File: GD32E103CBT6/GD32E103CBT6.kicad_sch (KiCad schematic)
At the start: 15 parts, among them J1 DBG, U1 GD32E103CBTx, Y1 16MHz

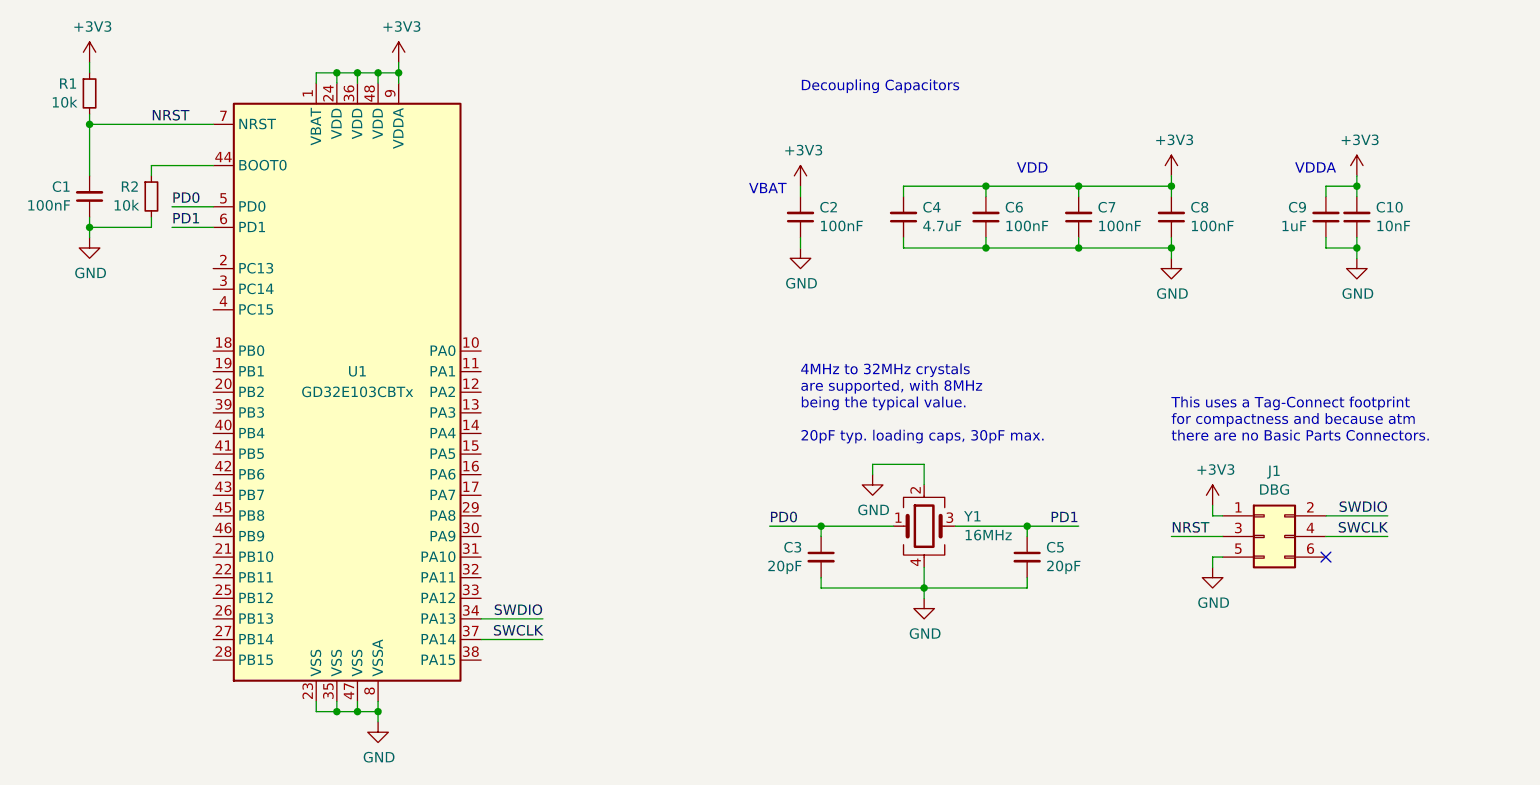
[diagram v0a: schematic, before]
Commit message: Revert "Update modules to kicad v7 format"
This reverts commit 3325eb02d48d3d222bc7f8945228a1814ae85736.
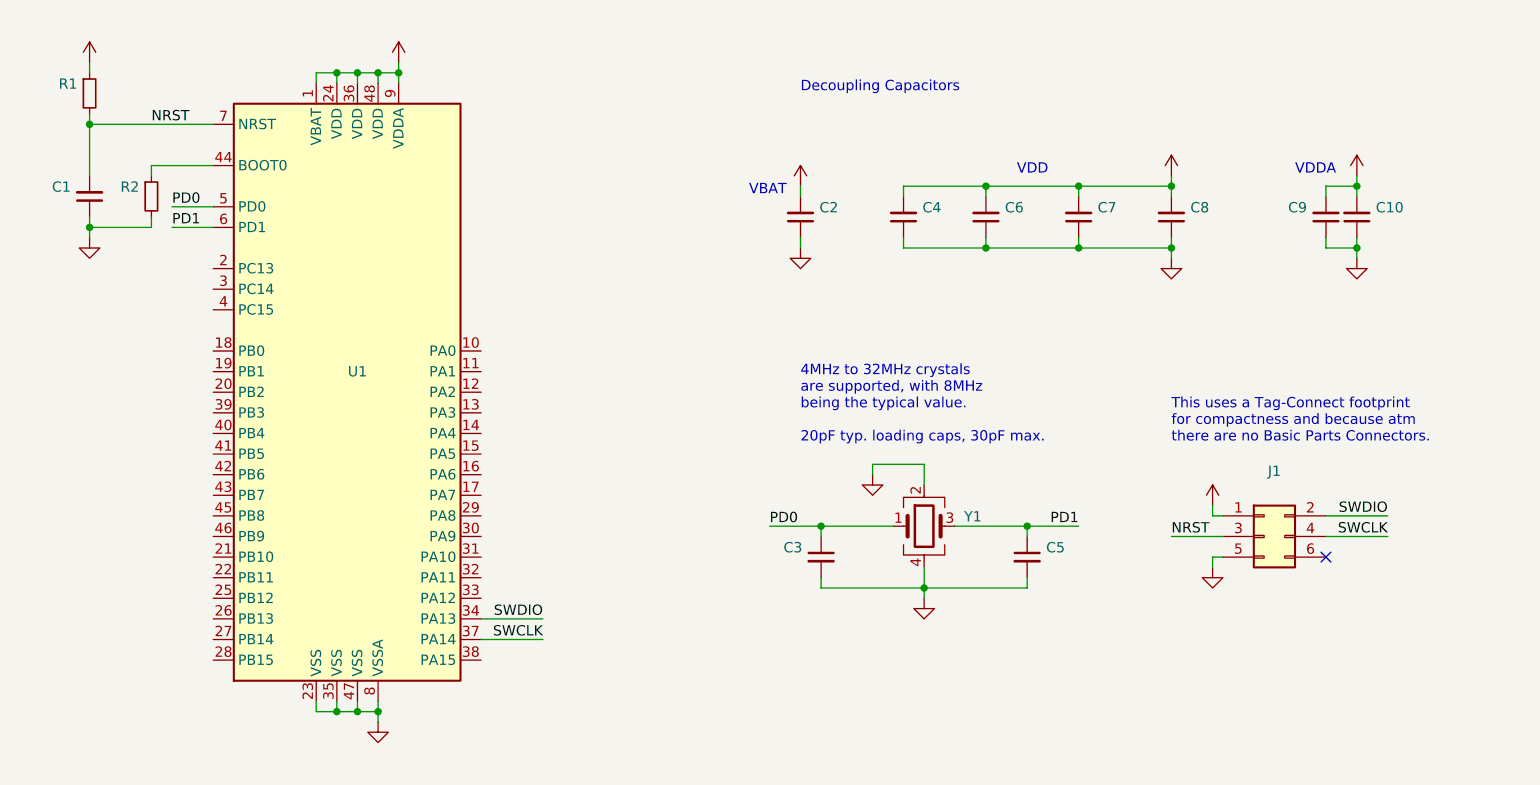
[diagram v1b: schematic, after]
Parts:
- C1, C2, C6, C7, C8: value 100nF -> (none); footprint Capacitor_SMD:C_0402_1005Metric -> (none)
- C10: value 10nF -> (none); footprint Capacitor_SMD:C_0402_1005Metric -> (none)
- C3, C5: value 20pF -> (none); footprint Capacitor_SMD:C_0402_1005Metric -> (none)
- C4: value 4.7uF -> (none); footprint Capacitor_SMD:C_0402_1005Metric -> (none)
- C9: value 1uF -> (none); footprint Capacitor_SMD:C_0402_1005Metric -> (none)
- J1: value DBG -> (none); footprint Connector:Tag-Connect_TC2030-IDC-NL_2x03_P1.27mm_Vertical -> (none)
- R1, R2: value 10k -> (none); footprint Resistor_SMD:R_0402_1005Metric -> (none)
- U1: value GD32E103CBTx -> (none); footprint Package_QFP:LQFP-48_7x7mm_P0.5mm -> (none)
- Y1: value 16MHz -> (none); footprint Crystal:Crystal_SMD_3225-4Pin_3.2x2.5mm -> (none)

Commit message: Reapply "Update modules to kicad v7 format"
This reverts commit fa5cc85431189ac7a3beedf0871b5723203ae43f.
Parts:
- C1, C2, C6, C7, C8: value (none) -> 100nF; footprint (none) -> Capacitor_SMD:C_0402_1005Metric
- C10: value (none) -> 10nF; footprint (none) -> Capacitor_SMD:C_0402_1005Metric
- C3, C5: value (none) -> 20pF; footprint (none) -> Capacitor_SMD:C_0402_1005Metric
- C4: value (none) -> 4.7uF; footprint (none) -> Capacitor_SMD:C_0402_1005Metric
- C9: value (none) -> 1uF; footprint (none) -> Capacitor_SMD:C_0402_1005Metric
- J1: value (none) -> DBG; footprint (none) -> Connector:Tag-Connect_TC2030-IDC-NL_2x03_P1.27mm_Vertical
- R1, R2: value (none) -> 10k; footprint (none) -> Resistor_SMD:R_0402_1005Metric
- U1: value (none) -> GD32E103CBTx; footprint (none) -> Package_QFP:LQFP-48_7x7mm_P0.5mm
- Y1: value (none) -> 16MHz; footprint (none) -> Crystal:Crystal_SMD_3225-4Pin_3.2x2.5mm
